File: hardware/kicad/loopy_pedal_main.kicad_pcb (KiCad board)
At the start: 2 copper layers, 82 x 66 mm, 76 parts, among them J1 USB_C_Receptacle_USB2.0_16P, J10 Conn_01x02, J11 Conn_01x03, J2 Barrel_Jack, J3 Conn_01x06, J4 Conn_01x06, J5 Conn_01x08, J6 Conn_02x03_Odd_Even, J7 Conn_02x03_Odd_Even, J8 DIN-5_180degree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

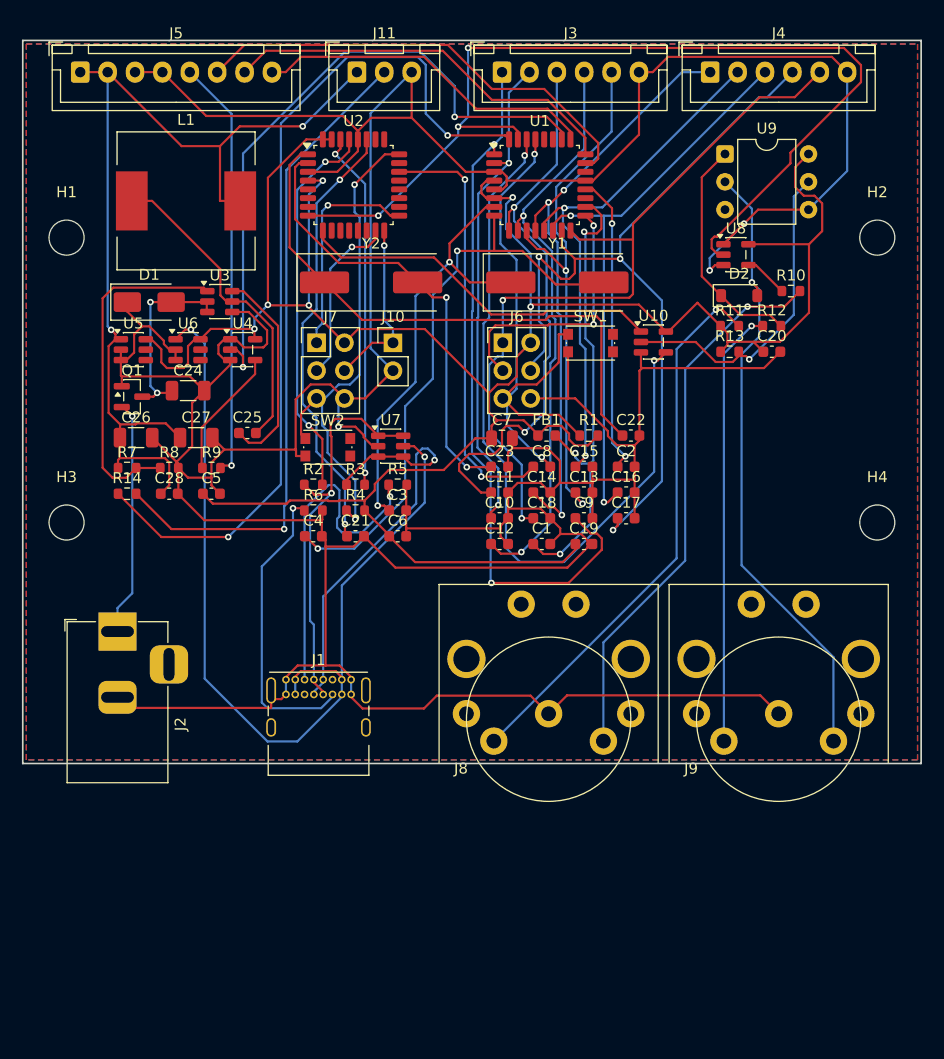
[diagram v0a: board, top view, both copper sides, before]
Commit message: feat(pcb): detailed DIN-5 socket model + reserve body clearance (82x70mm)
Model: rebuild the SDS-50J socket as separate coloured parts so the .wrl
carries real materials (STL drops colour). Black body, dark recessed plug
cavity with the 5 metal contacts in the DIN-5 fan + keyway notch, all 7 solder
pins and 2 plastic locating posts.

Layout: the right-angle DIN bodies reach ~20mm in from the bottom edge - deeper
than their courtyard reserved - so they overlapped the bottom row of parts
(C12/C1/C19). Grow the board 66->70mm to open a full-depth connector band; all
parts now clear the sockets. Re-placed and re-routed (Freerouting), DRC 0/0.
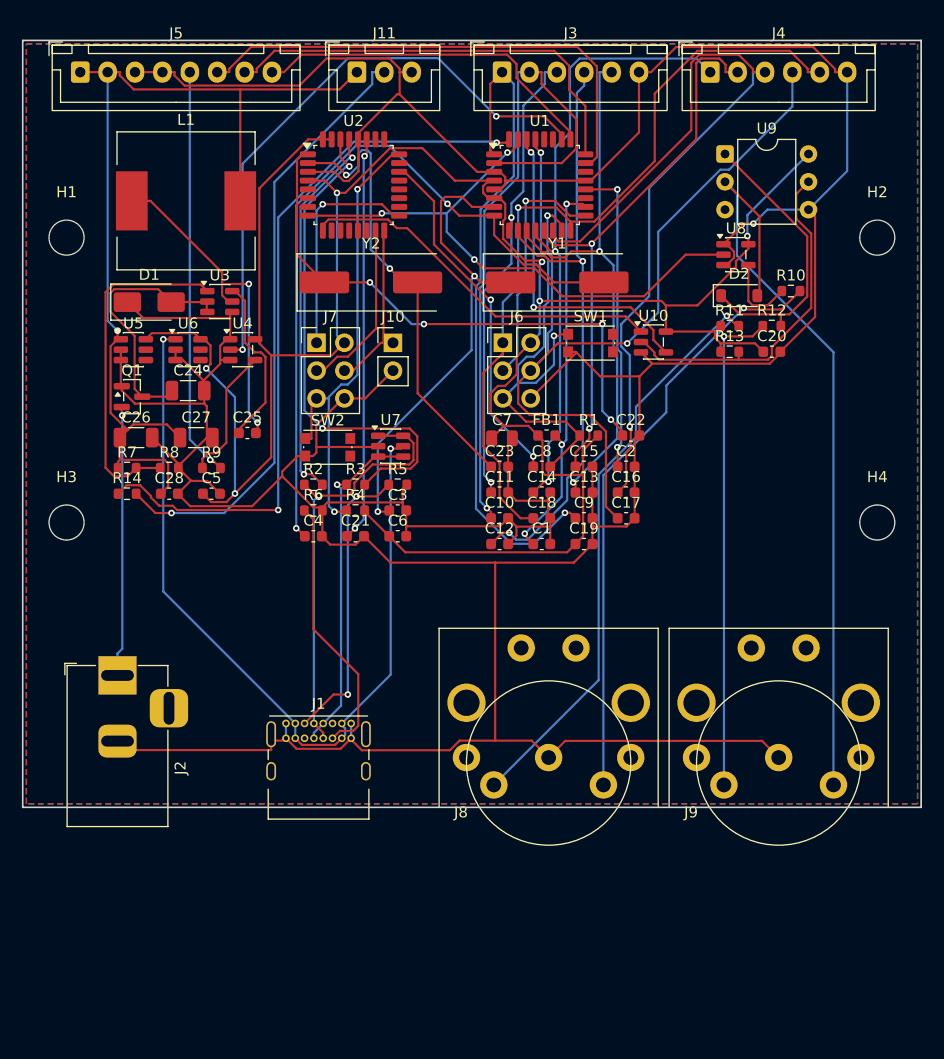
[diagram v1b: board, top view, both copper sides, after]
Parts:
- moved J1 4.00 mm to (54.0, 92.3)
- moved J2 4.00 mm to (38.6, 88.0)
- moved J8 4.00 mm to (78.0, 95.5)
- moved J9 4.00 mm to (99.0, 95.5)
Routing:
- net UART_RX: track 68.8 -> 29.9 mm
- net UART_TX: track 91.8 -> 53.3 mm
- net GND: track 471.3 -> 440.9 mm, vias 3 -> 1
- net SW_TRACK4: track 53.4 -> 76.9 mm, vias 2 -> 1
- net SW_STOP: track 45.1 -> 61.1 mm, vias 2 -> 1
- net IND_DATA: track 80.5 -> 66.8 mm
- net N$10: track 32.9 -> 46.2 mm
- net N$4: track 54.0 -> 67.1 mm
- net N$21: track 57.9 -> 70.9 mm, vias 1 -> 0
- net SW_UNDO: track 52.0 -> 43.3 mm
- net VBUS: track 84.7 -> 77.0 mm
- net N$1: track 43.2 -> 35.9 mm
- net DTR: track 39.2 -> 32.4 mm
- net USB_D-: track 38.2 -> 31.4 mm
- net +9V: track 17.6 -> 24.0 mm, vias 2 -> 0
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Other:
- board size 82 x 66 mm -> 82 x 70 mm

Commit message: fix(pcb): datasheet-accurate female DIN-5 socket (footprint + model)
Rebuild the SDS-50J footprint to the datasheet PCB-layout orientation: pins
1-2-3 in a horizontal 15mm row (Ø1.3), 4-5 above at +2.5 (10mm span), two
shield/earth tabs and two Ø2.4 mounting holes, socket opening facing +Y. This
fixes the 90deg-rotated placement (J8/J9 now placed at rot 0, spaced 22mm).

Rebuild the 3D model as a FEMALE socket in the correct WRL frame (verified with
an axis-marker probe: scad X->board X, Y->board Y out the edge, Z->up): recessed
Ø14 plug cavity with five female contact bores in the DIN-5 fan (pin 2 bottom,
keyway top) - no protruding male pins - plus the 7 solder tails and 2 posts.

J8/J9 re-imported with nets preserved; re-placed and re-routed at 0.18mm route
clearance (keeps Freerouting's optimiser off the 0.15mm DRC floor). DRC 0/0.
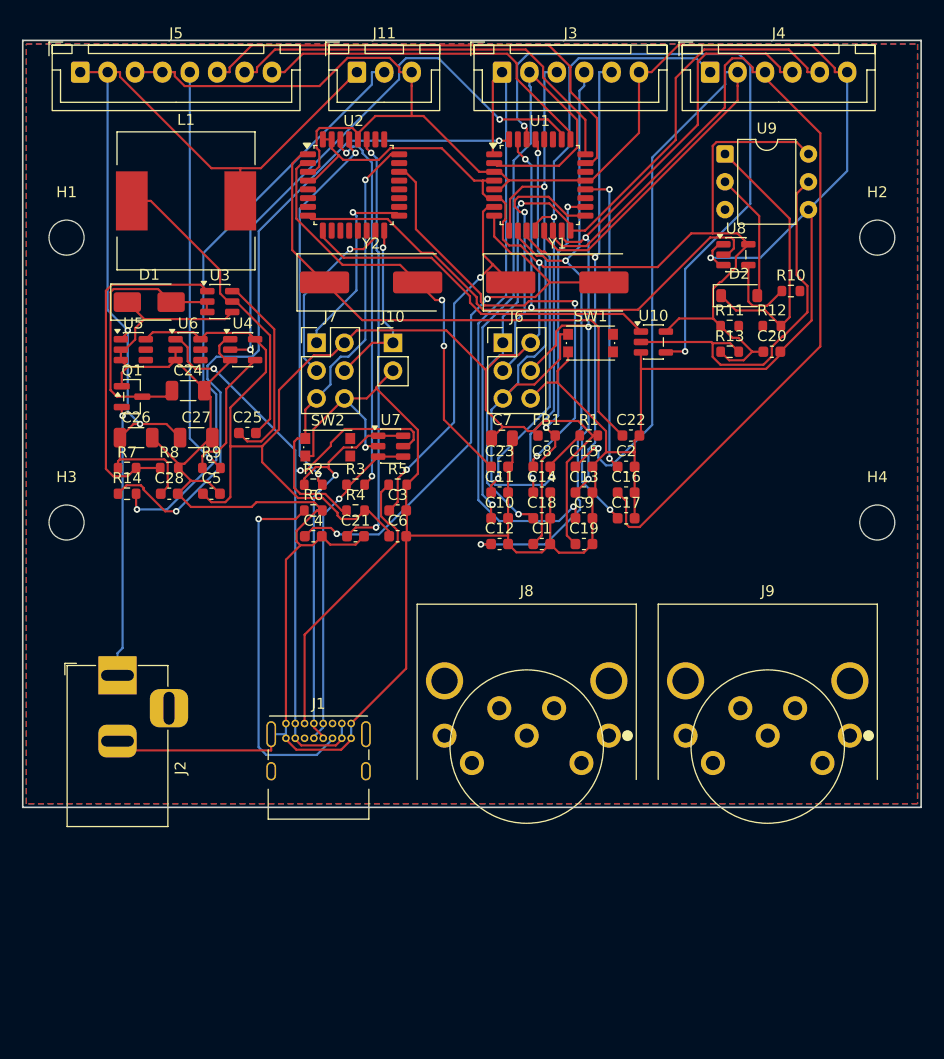
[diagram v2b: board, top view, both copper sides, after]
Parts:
- J8, J9: value DIN-5_180degree -> MIDI_DIN5_RA
- moved J8 2.83 mm to (76.0, 93.5), turned to 0 degrees
- moved J9 2.24 mm to (98.0, 93.5), turned to 0 degrees
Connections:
- J8 pad 2: GND -> (no net)
- J8 pad 4: N$18 -> (no net)
- J8 pad 5: N$17 -> (no net)
- J9 pad 2: GND -> (no net)
- J9 pad 4: N$19 -> (no net)
- J9 pad 5: N$21 -> (no net)
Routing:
- net N$21: track 70.9 -> 11.8 mm
- net N$17: track 54.7 -> 0.00 mm, vias 1 -> 0
- net N$18: track 53.1 -> 0.00 mm, vias 1 -> 0
- net N$19: track 44.9 -> 0.00 mm, vias 1 -> 0
- net GND: track 440.9 -> 406.7 mm, vias 1 -> 2
- net UART_RX: track 29.9 -> 59.7 mm
- net SW_TRACK3: track 51.5 -> 73.4 mm, vias 2 -> 1
- net N$4: track 67.1 -> 52.9 mm
- net VBUS: track 77.0 -> 63.0 mm
- net N$10: track 46.2 -> 34.5 mm
- net SW_CLEAR: track 79.5 -> 68.4 mm, vias 2 -> 3
- net +5V: track 225.2 -> 214.1 mm, vias 6 -> 1
- net UART_TX: track 53.3 -> 63.6 mm, vias 3 -> 2
- net SW_TRACK4: track 76.9 -> 85.6 mm, vias 1 -> 0
- net N$15: track 24.5 -> 33.0 mm, vias 0 -> 1
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
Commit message: fix(pcb): align DC/USB-C/MIDI connector faces coplanar at the edge
The three connector front faces protruded by different amounts (DC +1.7, USB-C
+0.9, MIDI +0.0 mm past the edge). Measured each footprint's face-to-courtyard
margin (barrel 0.29, USB-C 0.58, DIN 0.00) and tuned per-connector overhangs so
every face now lands 1.5 mm past the board edge. Re-placed and re-routed; DRC 0/0.
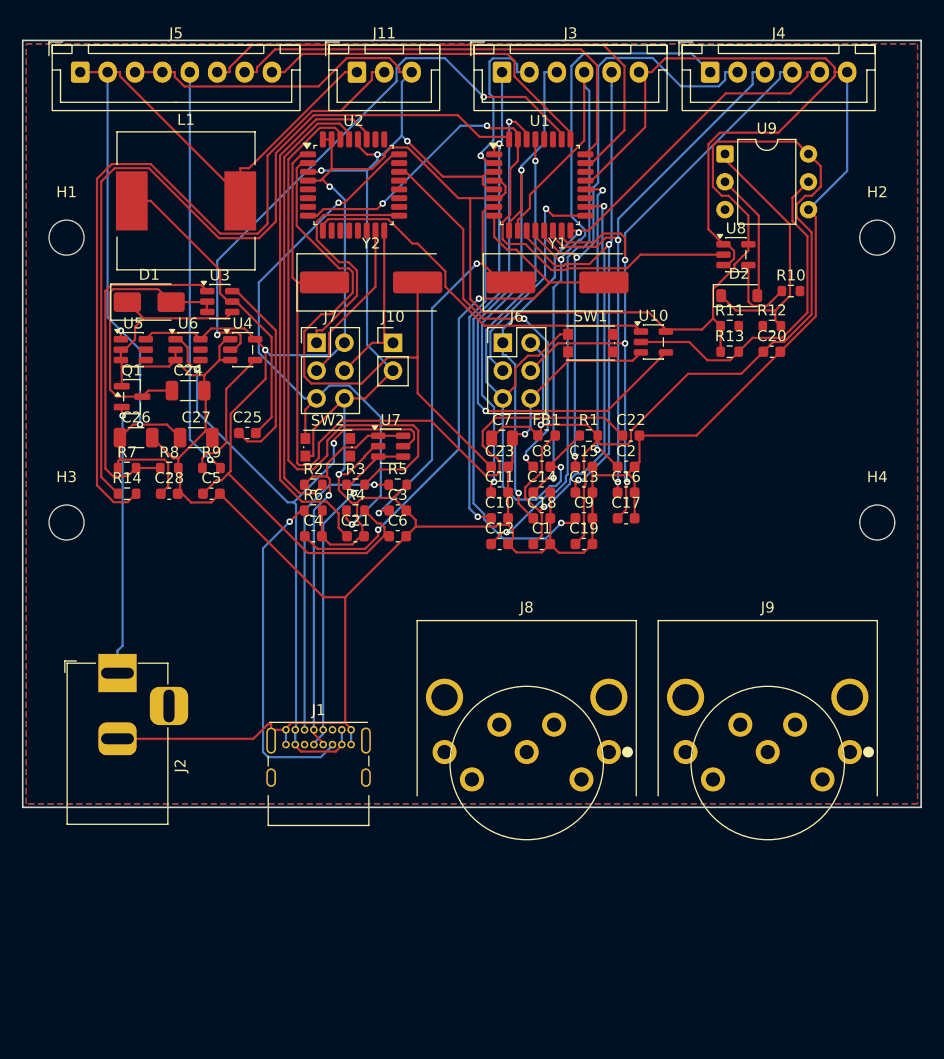
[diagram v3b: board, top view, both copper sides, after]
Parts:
- moved J8 1.50 mm to (76.0, 95.0)
- moved J9 1.50 mm to (98.0, 95.0)
- moved J1 0.58 mm to (54.0, 92.9)
- moved J2 0.21 mm to (38.6, 87.7)
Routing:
- net SW_TRACK4: track 85.6 -> 51.9 mm, vias 0 -> 2
- net +5V: track 214.1 -> 238.0 mm, vias 1 -> 3
- net N$10: track 34.5 -> 57.4 mm, vias 2 -> 0
- net N$7: track 51.3 -> 73.4 mm
- net IND_DATA_OUT: track 54.0 -> 72.1 mm, vias 1 -> 0
- net N$8: track 39.3 -> 56.4 mm, vias 2 -> 0
- net SW_TRACK3: track 73.4 -> 57.0 mm, vias 1 -> 2
- net IND_DATA: track 64.6 -> 78.7 mm, vias 2 -> 0
- net RST_16: track 41.3 -> 55.0 mm, vias 1 -> 2
- net SW_BANK: track 72.4 -> 59.4 mm
- net UART_RX: track 59.7 -> 49.1 mm
- net N$1: track 34.4 -> 44.7 mm
- net N$6: track 38.9 -> 49.0 mm, vias 2 -> 0
- net SW_STOP: track 60.1 -> 50.7 mm, vias 1 -> 2
- net UART_TX: track 63.6 -> 55.0 mm
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
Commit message: feat(pcb): one 2-pin JST-XH header per footswitch pedal
Replace the two aggregated 6-pin footswitch connectors (J3/J4) with ten
individual 2-pin JST-XH headers (J3, J4, J12-J19) - one per pedal, pin 1 =
switch signal, pin 2 = GND - so each footswitch plugs in on its own connector.

Schematic (main_board.py) + netlist regenerated (0 ERC errors). Board: headers
laid out in a 5x2 grid below the top connectors; board grew 82x70 -> 82x88 mm
(logic band shifted down, mounting holes repositioned). Re-placed and re-routed,
DRC 0/0. Doc updated with the ref->pedal mapping.
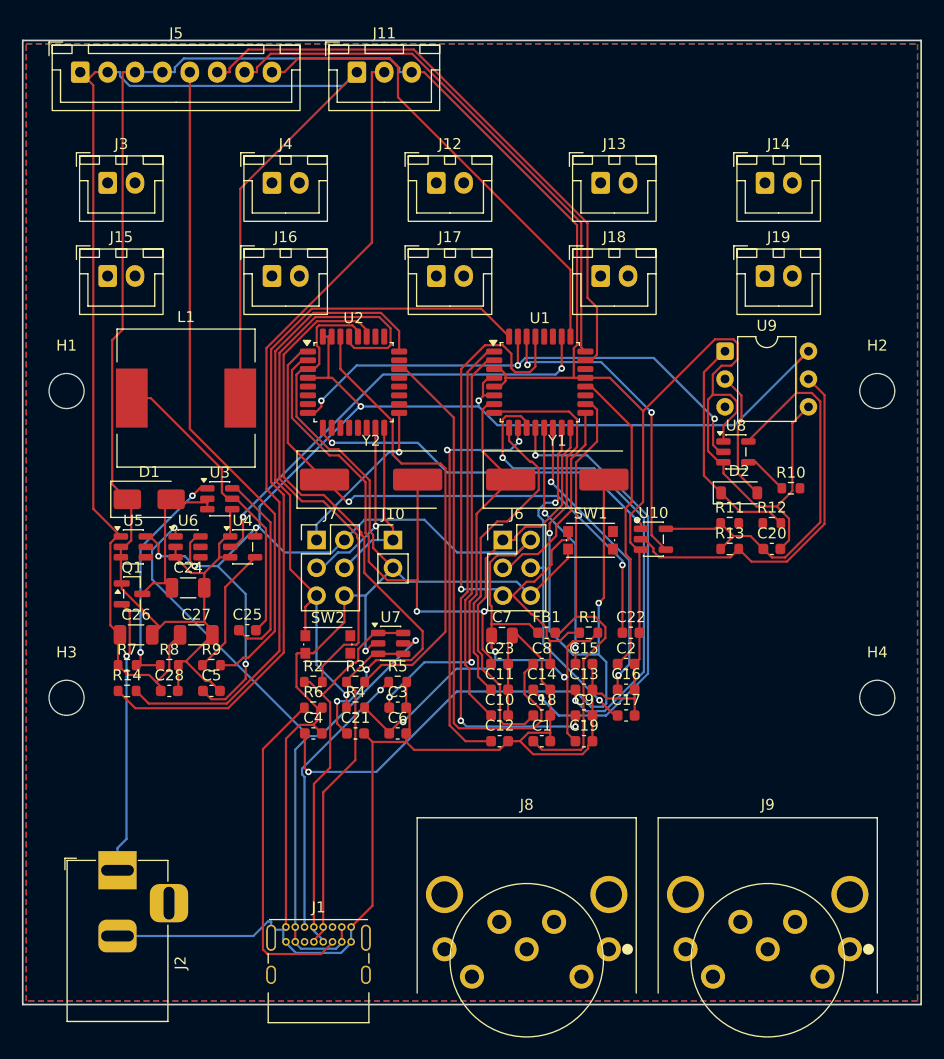
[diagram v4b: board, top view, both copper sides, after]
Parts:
- added J12: FSW_UNDO, JST_XH_B2B-XH-A_1x02_P2.50mm_Vertical, F.Cu at (67.8, 43.0)
- added J13: FSW_MODE, JST_XH_B2B-XH-A_1x02_P2.50mm_Vertical, F.Cu at (82.8, 43.0)
- added J14: FSW_TRACK1, JST_XH_B2B-XH-A_1x02_P2.50mm_Vertical, F.Cu at (97.8, 43.0)
- added J15: FSW_TRACK2, JST_XH_B2B-XH-A_1x02_P2.50mm_Vertical, F.Cu at (37.8, 51.5)
- added J16: FSW_TRACK3, JST_XH_B2B-XH-A_1x02_P2.50mm_Vertical, F.Cu at (52.8, 51.5)
- added J17: FSW_TRACK4, JST_XH_B2B-XH-A_1x02_P2.50mm_Vertical, F.Cu at (67.8, 51.5)
- added J18: FSW_CLEAR, JST_XH_B2B-XH-A_1x02_P2.50mm_Vertical, F.Cu at (82.8, 51.5)
- added J19: FSW_BANK, JST_XH_B2B-XH-A_1x02_P2.50mm_Vertical, F.Cu at (97.8, 51.5)
- J3: value Conn_01x06 -> FSW_RECPLAY; footprint JST_XH_B6B-XH-A_1x06_P2.50mm_Vertical -> JST_XH_B2B-XH-A_1x02_P2.50mm_Vertical
- J4: value Conn_01x06 -> FSW_STOP; footprint JST_XH_B6B-XH-A_1x06_P2.50mm_Vertical -> JST_XH_B2B-XH-A_1x02_P2.50mm_Vertical
- moved J4 41.3 mm to (52.8, 43.0)
- moved J3 37.4 mm to (37.8, 43.0)
- moved C20 18.0 mm to (98.4, 76.4)
- moved D1 18.0 mm to (41.5, 71.9)
- moved R13 18.0 mm to (94.5, 76.4)
- moved U10 18.0 mm to (87.6, 75.5)
- moved U8 18.0 mm to (95.1, 67.6)
- moved C1 18.0 mm to (77.4, 94.0)
- moved C10 18.0 mm to (73.5, 91.6)
- moved C11 18.0 mm to (73.5, 89.3)
- moved C12 18.0 mm to (73.5, 94.0)
- moved C13 18.0 mm to (81.2, 89.3)
- moved C14 18.0 mm to (77.4, 89.3)
- moved C15 18.0 mm to (81.2, 86.9)
- moved C16 18.0 mm to (85.1, 89.3)
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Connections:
- J3 pad 1: SW_RECPLAY -> (no net)
- J3 pad 2: SW_STOP -> (no net)
- J4 pad 1: SW_TRACK2 -> (no net)
- J4 pad 2: SW_TRACK3 -> (no net)
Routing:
- net GND: track 413.9 -> 457.5 mm, vias 5 -> 1
- net +5V_LED: track 87.4 -> 127.2 mm, vias 2 -> 0
- net N$4: track 53.9 -> 89.1 mm, vias 2 -> 3
- net SW_CLEAR: track 66.9 -> 31.9 mm, vias 3 -> 2
- net SW_TRACK3: track 57.0 -> 22.7 mm
- net SW_MODE: track 64.9 -> 37.8 mm, vias 1 -> 2
- net SW_TRACK4: track 51.9 -> 27.4 mm
- net SW_BANK: track 59.4 -> 36.2 mm, vias 2 -> 0
- net RING_DATA_OUT: track 37.4 -> 60.5 mm, vias 1 -> 0
- net N$7: track 73.4 -> 51.4 mm, vias 0 -> 2
- net UART_RX: track 49.1 -> 29.0 mm
- net SW_UNDO: track 48.4 -> 28.8 mm, vias 2 -> 0
- net SW_TRACK2: track 59.4 -> 42.5 mm
- net SW_STOP: track 50.7 -> 34.8 mm, vias 2 -> 0
- net N$10: track 57.4 -> 42.3 mm
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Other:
- board size 82 x 70 mm -> 82 x 88 mm
